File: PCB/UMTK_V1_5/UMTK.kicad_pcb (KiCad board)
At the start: 4 copper layers, 170 x 80 mm, 99 parts, among them J1 Motor Out, J2 ESTOP, J3 LOADCELL, J5 PJ-102BH, J8 10033526-N3212LF, Q1 Q_PNP_BEC, U1 DRV8873SPWPRQ1, U10 LM2576HVS-5, U11 SN74LVC1T45DCK, U12 SN74LVC1T45DCK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

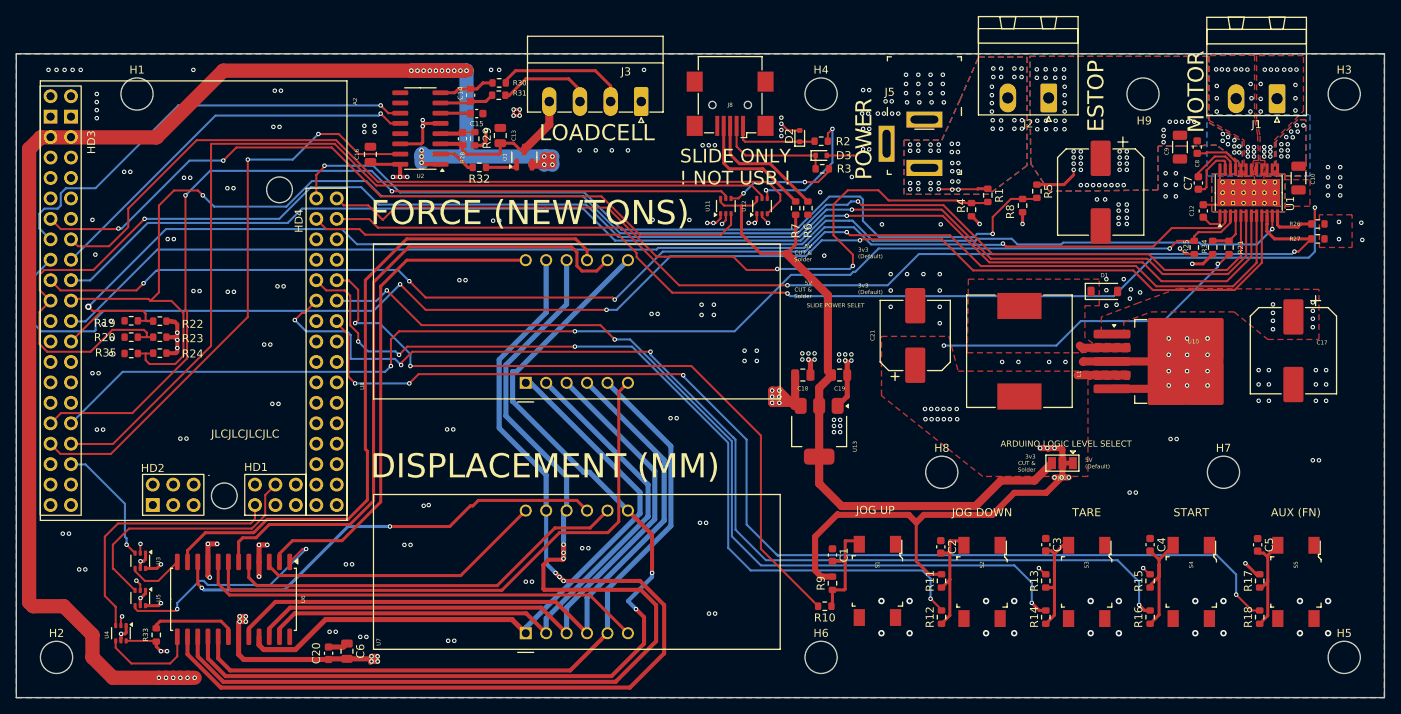
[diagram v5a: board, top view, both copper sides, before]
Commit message: Cleanup and update PCB
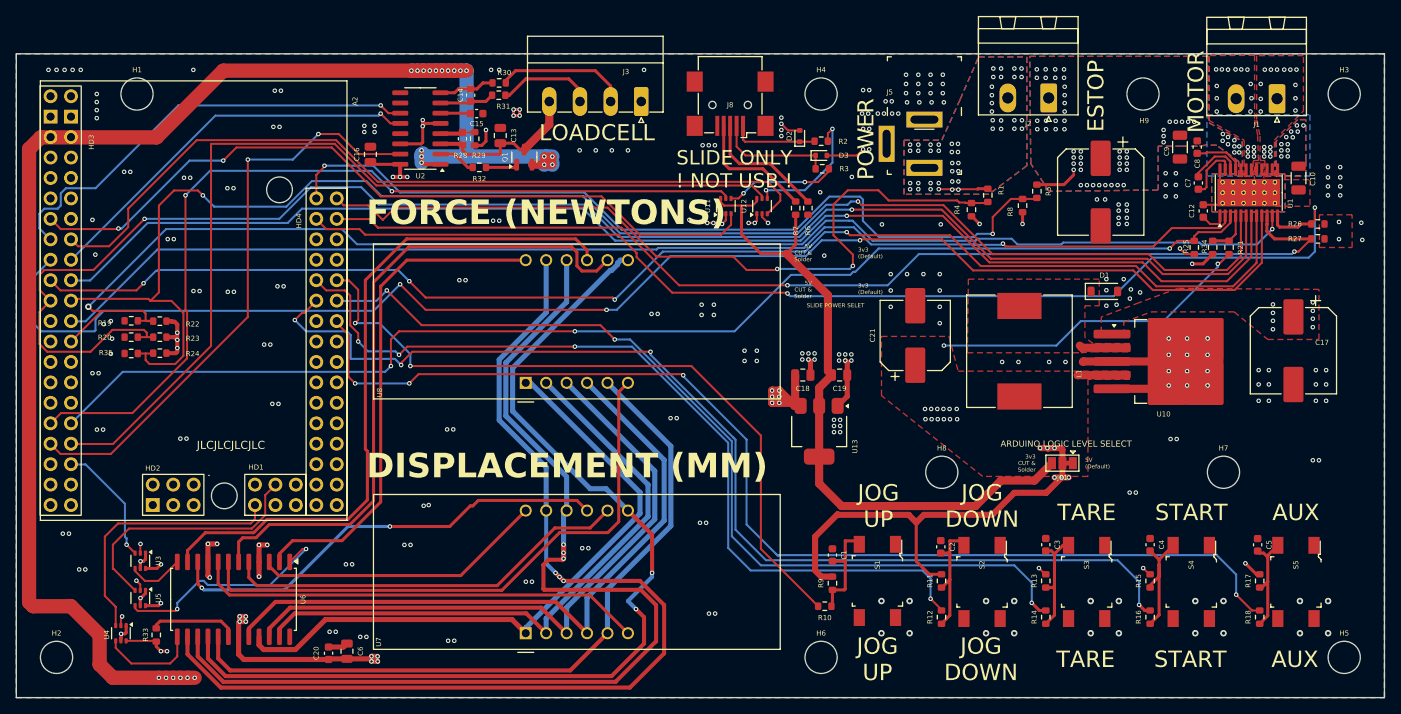
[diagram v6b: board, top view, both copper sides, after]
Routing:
- net Net-(U6-SEG_B): track 122.3 -> 123.3 mm
- net Net-(C3-Pad2): track 14.1 -> 13.3 mm
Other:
- board text added: "AUX"
- board text removed: "AUX (FN)"
